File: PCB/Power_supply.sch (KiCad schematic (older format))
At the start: 20 parts

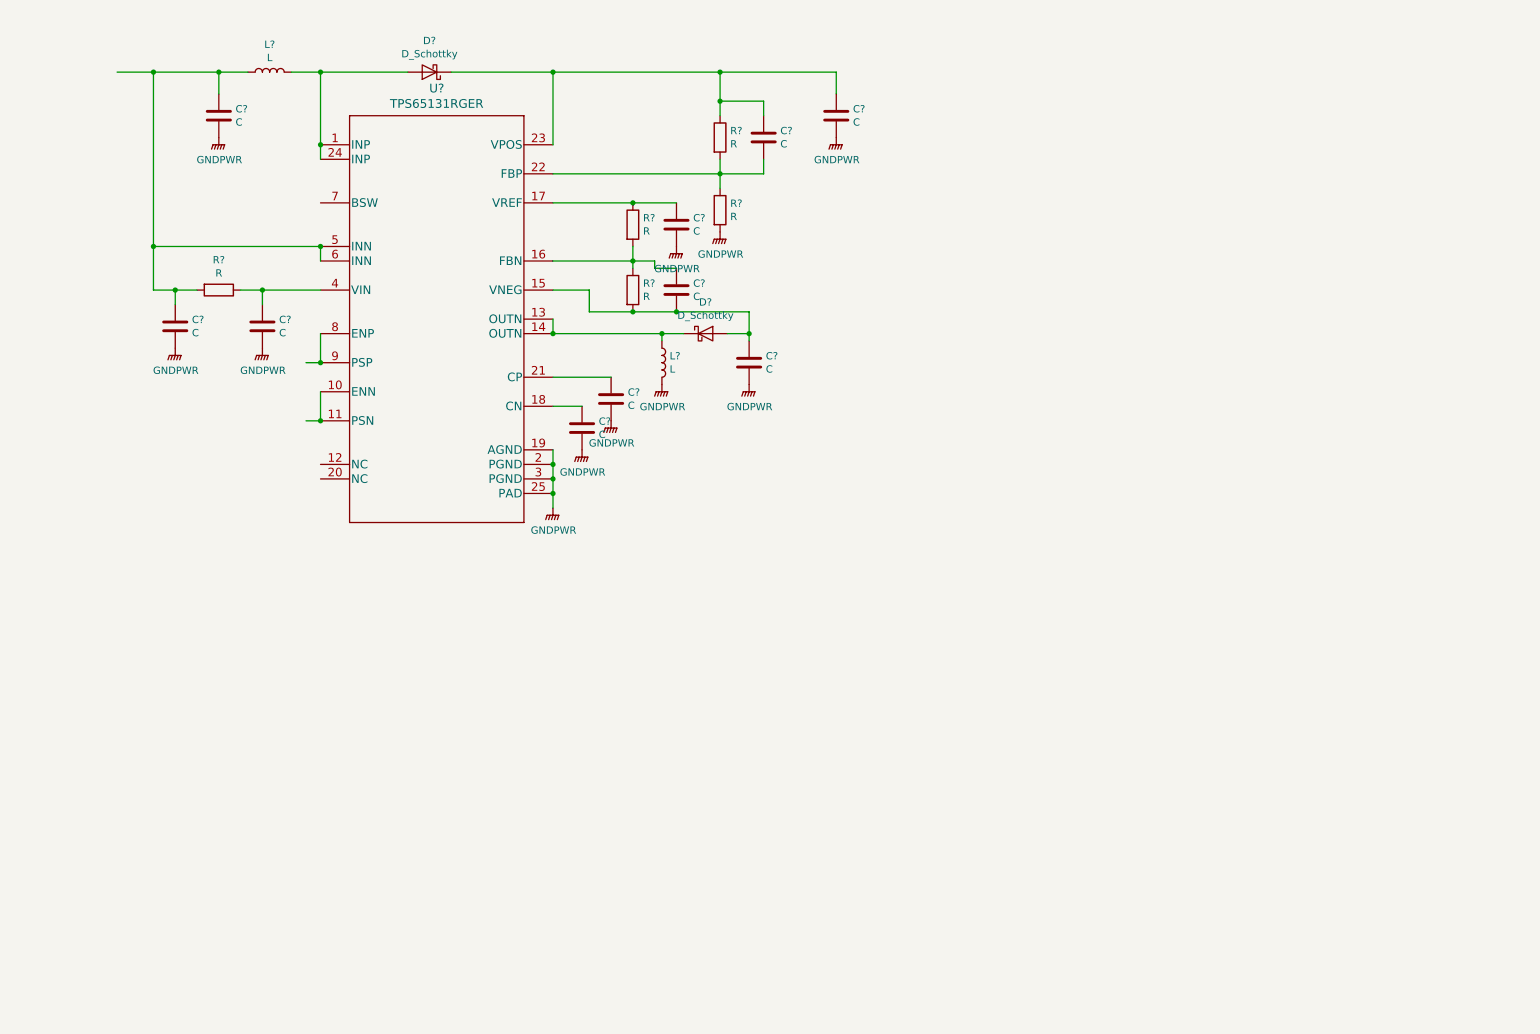
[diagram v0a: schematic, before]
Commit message: Added USB footprint and modified schematic
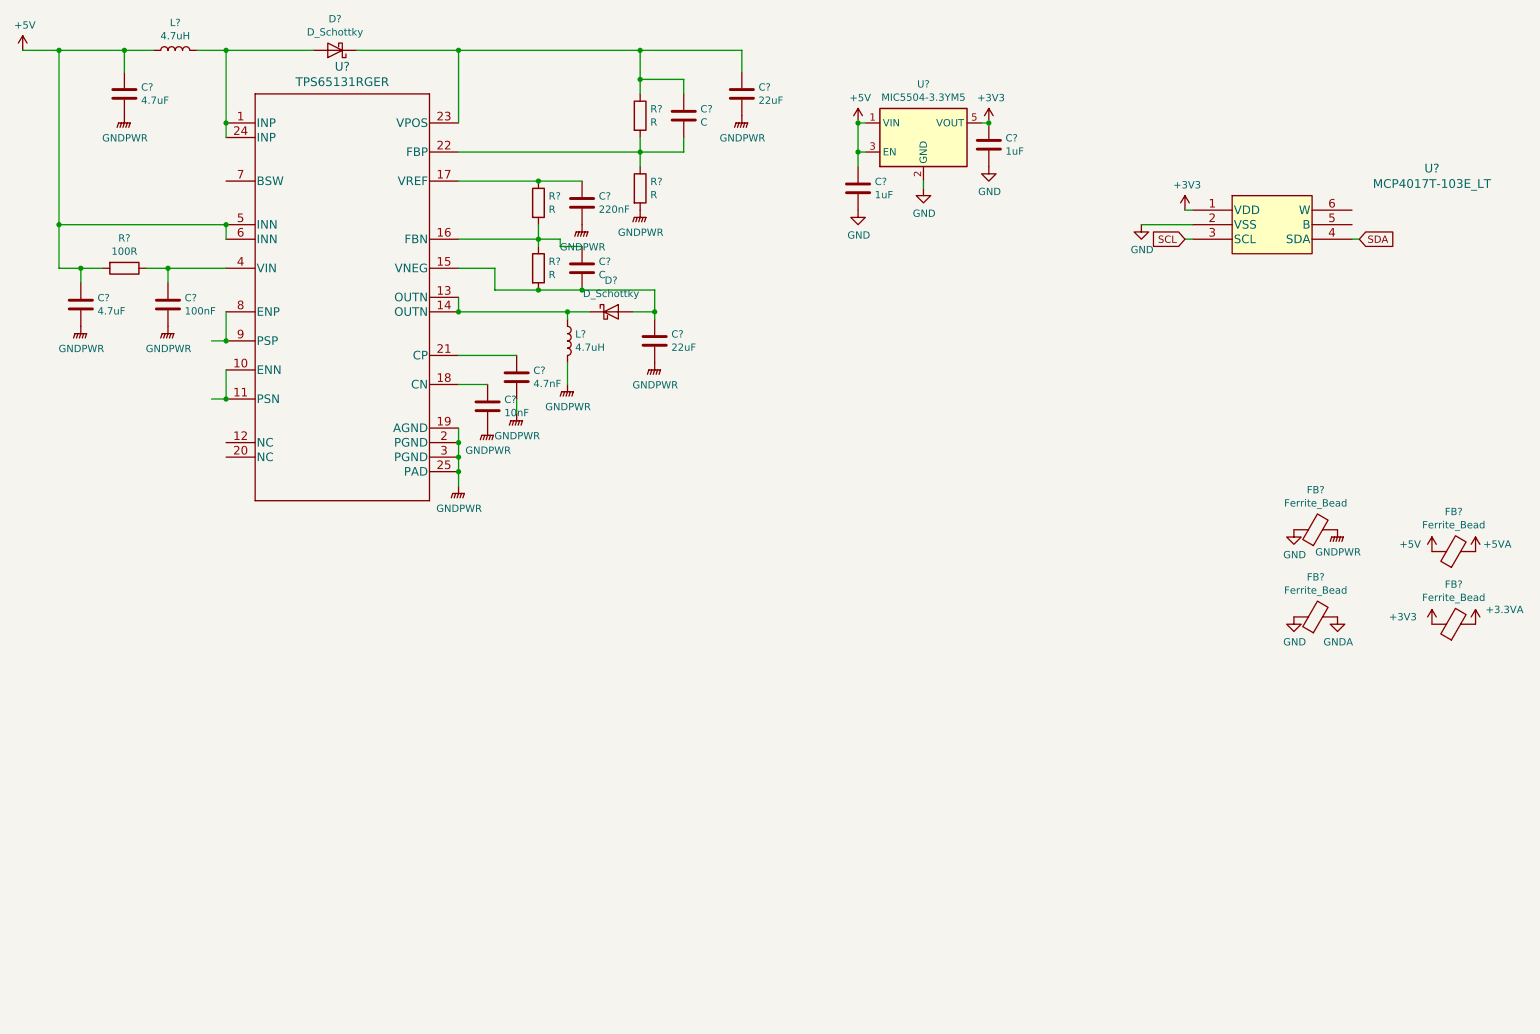
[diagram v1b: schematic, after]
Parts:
- added C? (x2): 1uF, symbol Device:C
- added FB? (x4): Ferrite_Bead, symbol Device:Ferrite_Bead
- added U?: MCP4017T-103E_LT, SC70-6_MC, symbol MCP4017T:MCP4017T-103E_LT
- added U?: MIC5504-3.3YM5, Package_TO_SOT_SMD:SOT-23-5, symbol Regulator_Linear:MIC5504-3.3YM5
- C?: value C -> 220nF
- C? (x2): value C -> 22uF
- C?: value C -> 4.7nF
- C?: value C -> 10nF
- C?: value C -> 100nF
- C? (x2): value C -> 4.7uF
- L? (x2): value L -> 4.7uH
- R?: value R -> 100R
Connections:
- net labels added: +3.3VA, +3V3, +5V, +5VA, GND, GNDA, SCL, SDA
- wire segments 62 -> 74
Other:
- moved on the sheet: C?, D?, L?, R?, U?

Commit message: Advancing in the schmatic. Power to be finished
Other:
- moved on the sheet: C?, U?
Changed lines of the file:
@@
 EESchema Schematic File Version 4
-LIBS:SquareLab-cache
 EELAYER 30 0
 EELAYER END
 $Descr A4 11693 8268
 encoding utf-8
-Sheet 3 3
+Sheet 2 3
 Title ""
 Date ""
@@
 L Regulator_Linear:MIC5504-3.3YM5 U?
 U 1 1 5E8EC3E8
-P 6950 1400
-F 0 "U?" H 6950 1767 50  0000 C CNN
-F 1 "MIC5504-3.3YM5" H 6950 1676 50  0000 C CNN
-F 2 "Package_TO_SOT_SMD:SOT-23-5" H 6950 1000 50  0001 C CNN
-F 3 "http://ww1.microchip.com/downloads/en/DeviceDoc/MIC550X.pdf" H 6700 1650 50  0001 C CNN
-	1    6950 1400
+P 7300 1450
+F 0 "U?" H 7300 1817 50  0000 C CNN
+F 1 "MIC5504-3.3YM5" H 7300 1726 50  0000 C CNN
+F 2 "Package_TO_SOT_SMD:SOT-23-5" H 7300 1050 50  0001 C CNN
+F 3 "http://ww1.microchip.com/downloads/en/DeviceDoc/MIC550X.pdf" H 7050 1700 50  0001 C CNN
+	1    7300 1450
 	1    0    0    -1
 $EndComp
@@
 L power:+5V #PWR0143
 U 1 1 5E8ECE98
-P 6500 1300
-F 0 "#PWR0143" H 6500 1150 50  0001 C CNN
-F 1 "+5V" H 6515 1473 50  0000 C CNN
-F 2 "" H 6500 1300 50  0001 C CNN
-F 3 "" H 6500 1300 50  0001 C CNN
-	1    6500 1300
+P 6700 1350
+F 0 "#PWR0143" H 6700 1200 50  0001 C CNN
+F 1 "+5V" H 6715 1523 50  0000 C CNN
+F 2 "" H 6700 1350 50  0001 C CNN
+F 3 "" H 6700 1350 50  0001 C CNN
+	1    6700 1350
 	1    0    0    -1
 $EndComp
@@
 L power:GND #PWR0144
 U 1 1 5E8EEBF1
-P 6950 1750
-F 0 "#PWR0144" H 6950 1500 50  0001 C CNN
-F 1 "GND" H 6955 1577 50  0000 C CNN
-F 2 "" H 6950 1750 50  0001 C CNN
-F 3 "" H 6950 1750 50  0001 C CNN
-	1    6950 1750
-	1    0    0    -1
-$EndComp
-Wire Wire Line
-	6950 1700 6950 1750
-Wire Wire Line
-	6500 1300 6550 1300
+P 7300 1800
+F 0 "#PWR0144" H 7300 1550 50  0001 C CNN
+F 1 "GND" H 7305 1627 50  0000 C CNN
+F 2 "" H 7300 1800 50  0001 C CNN
+F 3 "" H 7300 1800 50  0001 C CNN
+	1    7300 1800
+	1    0    0    -1
+$EndComp
+Wire Wire Line
+	7300 1750 7300 1800
 $Comp
 L power:+3V3 #PWR0145
 U 1 1 5E8F1113
-P 7400 1300
-F 0 "#PWR0145" H 7400 1150 50  0001 C CNN
-F 1 "+3V3" H 7415 1473 50  0000 C CNN
-F 2 "" H 7400 1300 50  0001 C CNN
-F 3 "" H 7400 1300 50  0001 C CNN
-	1    7400 1300
-	1    0    0    -1
-$EndComp
-Wire Wire Line
-	7350 1300 7400 1300
-Wire Wire Line
-	6550 1500 6500 1500
-Wire Wire Line
-	6500 1500 6500 1300
-Connection ~ 6500 1300
+P 7900 1350
+F 0 "#PWR0145" H 7900 1200 50  0001 C CNN
+F 1 "+3V3" H 7915 1523 50  0000 C CNN
+F 2 "" H 7900 1350 50  0001 C CNN
+F 3 "" H 7900 1350 50  0001 C CNN
+	1    7900 1350
+	1    0    0    -1
+$EndComp
+Wire Wire Line
+	6700 1550 6700 1350
+Connection ~ 6700 1350
 $Comp
 L Device:C C?
 U 1 1 5E8F4649
-P 6500 1750
-F 0 "C?" H 6615 1796 50  0000 L CNN
-F 1 "1uF" H 6615 1705 50  0000 L CNN
-F 2 "" H 6538 1600 50  0001 C CNN
-F 3 "~" H 6500 1750 50  0001 C CNN
-	1    6500 1750
-	1    0    0    -1
-$EndComp
-Connection ~ 6500 1500
+P 6700 1800
+F 0 "C?" H 6815 1846 50  0000 L CNN
+F 1 "1uF" H 6815 1755 50  0000 L CNN
+F 2 "" H 6738 1650 50  0001 C CNN
+F 3 "~" H 6700 1800 50  0001 C CNN
+	1    6700 1800
+	1    0    0    -1
+$EndComp
+Connection ~ 6700 1550
 $Comp
 L Device:C C?
 U 1 1 5E8F49CD
-P 7400 1450
-F 0 "C?" H 7515 1496 50  0000 L CNN
-F 1 "1uF" H 7515 1405 50  0000 L CNN
-F 2 "" H 7438 1300 50  0001 C CNN
-F 3 "~" H 7400 1450 50  0001 C CNN
-	1    7400 1450
-	1    0    0    -1
-$EndComp
-Connection ~ 7400 1300
-Wire Wire Line
-	6500 1500 6500 1600
+P 7900 1500
+F 0 "C?" H 8015 1546 50  0000 L CNN
+F 1 "1uF" H 8015 1455 50  0000 L CNN
+F 2 "" H 7938 1350 50  0001 C CNN
+F 3 "~" H 7900 1500 50  0001 C CNN
+	1    7900 1500
+	1    0    0    -1
+$EndComp
+Connection ~ 7900 1350
+Wire Wire Line
+	6700 1550 6700 1650
 $Comp
 L power:GND #PWR0146
 U 1 1 5E8F6E90
-P 6500 1900
-F 0 "#PWR0146" H 6500 1650 50  0001 C CNN
-F 1 "GND" H 6505 1727 50  0000 C CNN
-F 2 "" H 6500 1900 50  0001 C CNN
-F 3 "" H 6500 1900 50  0001 C CNN
-	1    6500 1900
+P 6700 1950
+F 0 "#PWR0146" H 6700 1700 50  0001 C CNN
+F 1 "GND" H 6705 1777 50  0000 C CNN
+F 2 "" H 6700 1950 50  0001 C CNN
+F 3 "" H 6700 1950 50  0001 C CNN
+	1    6700 1950
 	1    0    0    -1
 $EndComp
@@
 L power:GND #PWR0147
 U 1 1 5E8F7525
-P 7400 1600
-F 0 "#PWR0147" H 7400 1350 50  0001 C CNN
-F 1 "GND" H 7405 1427 50  0000 C CNN
-F 2 "" H 7400 1600 50  0001 C CNN
-F 3 "" H 7400 1600 50  0001 C CNN
-	1    7400 1600
+P 7900 1650
+F 0 "#PWR0147" H 7900 1400 50  0001 C CNN
+F 1 "GND" H 7905 1477 50  0000 C CNN
+F 2 "" H 7900 1650 50  0001 C CNN
+F 3 "" H 7900 1650 50  0001 C CNN
+	1    7900 1650
 	1    0    0    -1
 $EndComp
@@
 L MCP4017T:MCP4017T-103E_LT U?
 U 1 1 5E8A84B4
-P 9350 2000
-F 0 "U?" H 10450 2387 60  0000 C CNN
-F 1 "MCP4017T-103E_LT" H 10450 2281 60  0000 C CNN
-F 2 "SC70-6_MC" H 10450 2240 60  0001 C CNN
-F 3 "" H 9350 2000 60  0000 C CNN
-	1    9350 2000
-	1    0    0    -1
-$EndComp
-Text GLabel 9950 2100 2    50   Input ~ 0
-SDA
-Text GLabel 8750 2100 0    50   Input ~ 0
-SCL
+P 9600 1500
+F 0 "U?" H 9600 1850 60  0000 C CNN
+F 1 "MCP4017T-103E_LT" H 9600 1750 60  0000 C CNN
+F 2 "SC70-6_MC" H 10700 1740 60  0001 C CNN
+F 3 "" H 9600 1500 60  0000 C CNN
+	1    9600 1500
+	1    0    0    -1
+$EndComp
 $Comp
 L power:GND #PWR0156
 U 1 1 5E8CA208
-P 8450 2000
-F 0 "#PWR0156" H 8450 1750 50  0001 C CNN
-F 1 "GND" H 8455 1827 50  0000 C CNN
-F 2 "" H 8450 2000 50  0001 C CNN
-F 3 "" H 8450 2000 50  0001 C CNN
-	1    8450 2000
-	1    0    0    -1
-$EndComp
-Wire Wire Line
-	8750 2100 8800 2100
-Wire Wire Line
-	9900 2100 9950 2100
-Wire Wire Line
-	8450 2000 8800 2000
+P 8700 1500
+F 0 "#PWR0156" H 8700 1250 50  0001 C CNN
+F 1 "GND" H 8705 1327 50  0000 C CNN
+F 2 "" H 8700 1500 50  0001 C CNN
+F 3 "" H 8700 1500 50  0001 C CNN
+	1    8700 1500
+	1    0    0    -1
+$EndComp
+Wire Wire Line
+	9000 1600 9050 1600
+Wire Wire Line
+	10150 1600 10200 1600
+Wire Wire Line
+	8700 1500 9050 1500
 $Comp
 L power:+3V3 #PWR0157
 U 1 1 5E8D1F6A
-P 8750 1900
-F 0 "#PWR0157" H 8750 1750 50  0001 C CNN
-F 1 "+3V3" H 8765 2073 50  0000 C CNN
-F 2 "" H 8750 1900 50  0001 C CNN
-F 3 "" H 8750 1900 50  0001 C CNN
-	1    8750 1900
-	1    0    0    -1
-$EndComp
-Wire Wire Line
-	8750 1900 8800 1900
+P 9000 1400
+F 0 "#PWR0157" H 9000 1250 50  0001 C CNN
+F 1 "+3V3" H 8950 1600 50  0000 C CNN
+F 2 "" H 9000 1400 50  0001 C CNN
+F 3 "" H 9000 1400 50  0001 C CNN
+	1    9000 1400
+	1    0    0    -1
+$EndComp
+Wire Wire Line
+	9000 1400 9050 1400
 Wire Wire Line
 	4500 2950 4500 3100
@@
 Wire Wire Line
 	3750 1500 5000 1500
+Wire Wire Line
+	6700 1350 6900 1350
+Wire Wire Line
+	6700 1550 6900 1550
+Wire Wire Line
+	7700 1350 7900 1350
+Text HLabel 9000 1600 0    50   Input ~ 0
+SCL
+Text HLabel 10200 1600 2    50   Input ~ 0
+SDA
 $EndSCHEMATC

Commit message: Changed microcontroller, schemtic modified
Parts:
- removed R? (x2): R, symbol Device:R
- added C?: C, symbol Device:C
- added R?: R, symbol Device:R
- added U?: MCP4652T-104E_MF, symbol MCP46X1:MCP4652T-104E_MF
- added U?: TLV75901PDRVR, symbol TLV579:TLV75901PDRVR
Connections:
- net labels added: bottom_fb_res_n, bottom_fb_res_p, digipot_ldo, power_ldo_enable, power_switch_enable, vref
- wire segments 74 -> 105
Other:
- moved on the sheet: C?, D?, FB?, L?, R?, U?
